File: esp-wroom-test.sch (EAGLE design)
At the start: 27 parts, among them IC1 TCAN1051HGV, U1 NCP1117LPST50T3G, U2 XN04312, U8 NCP1117LPST50T3G

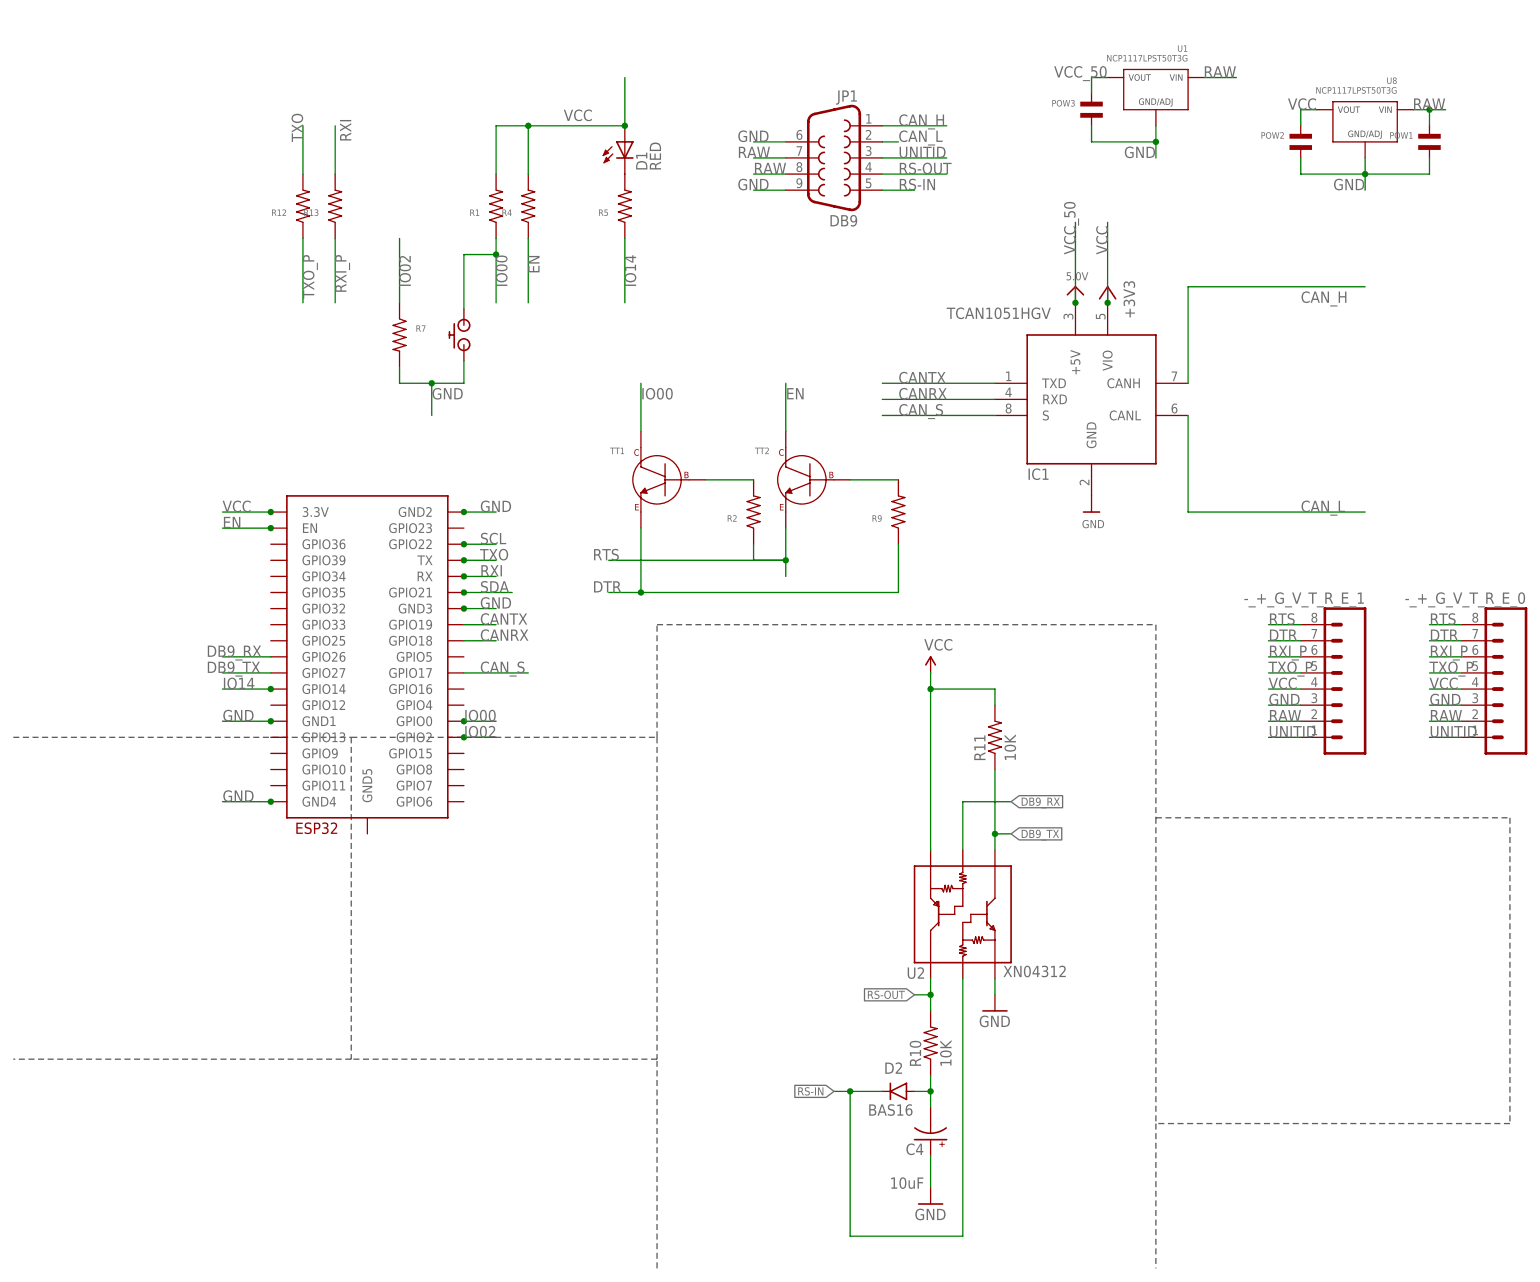
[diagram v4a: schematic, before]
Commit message: wroom test two sided
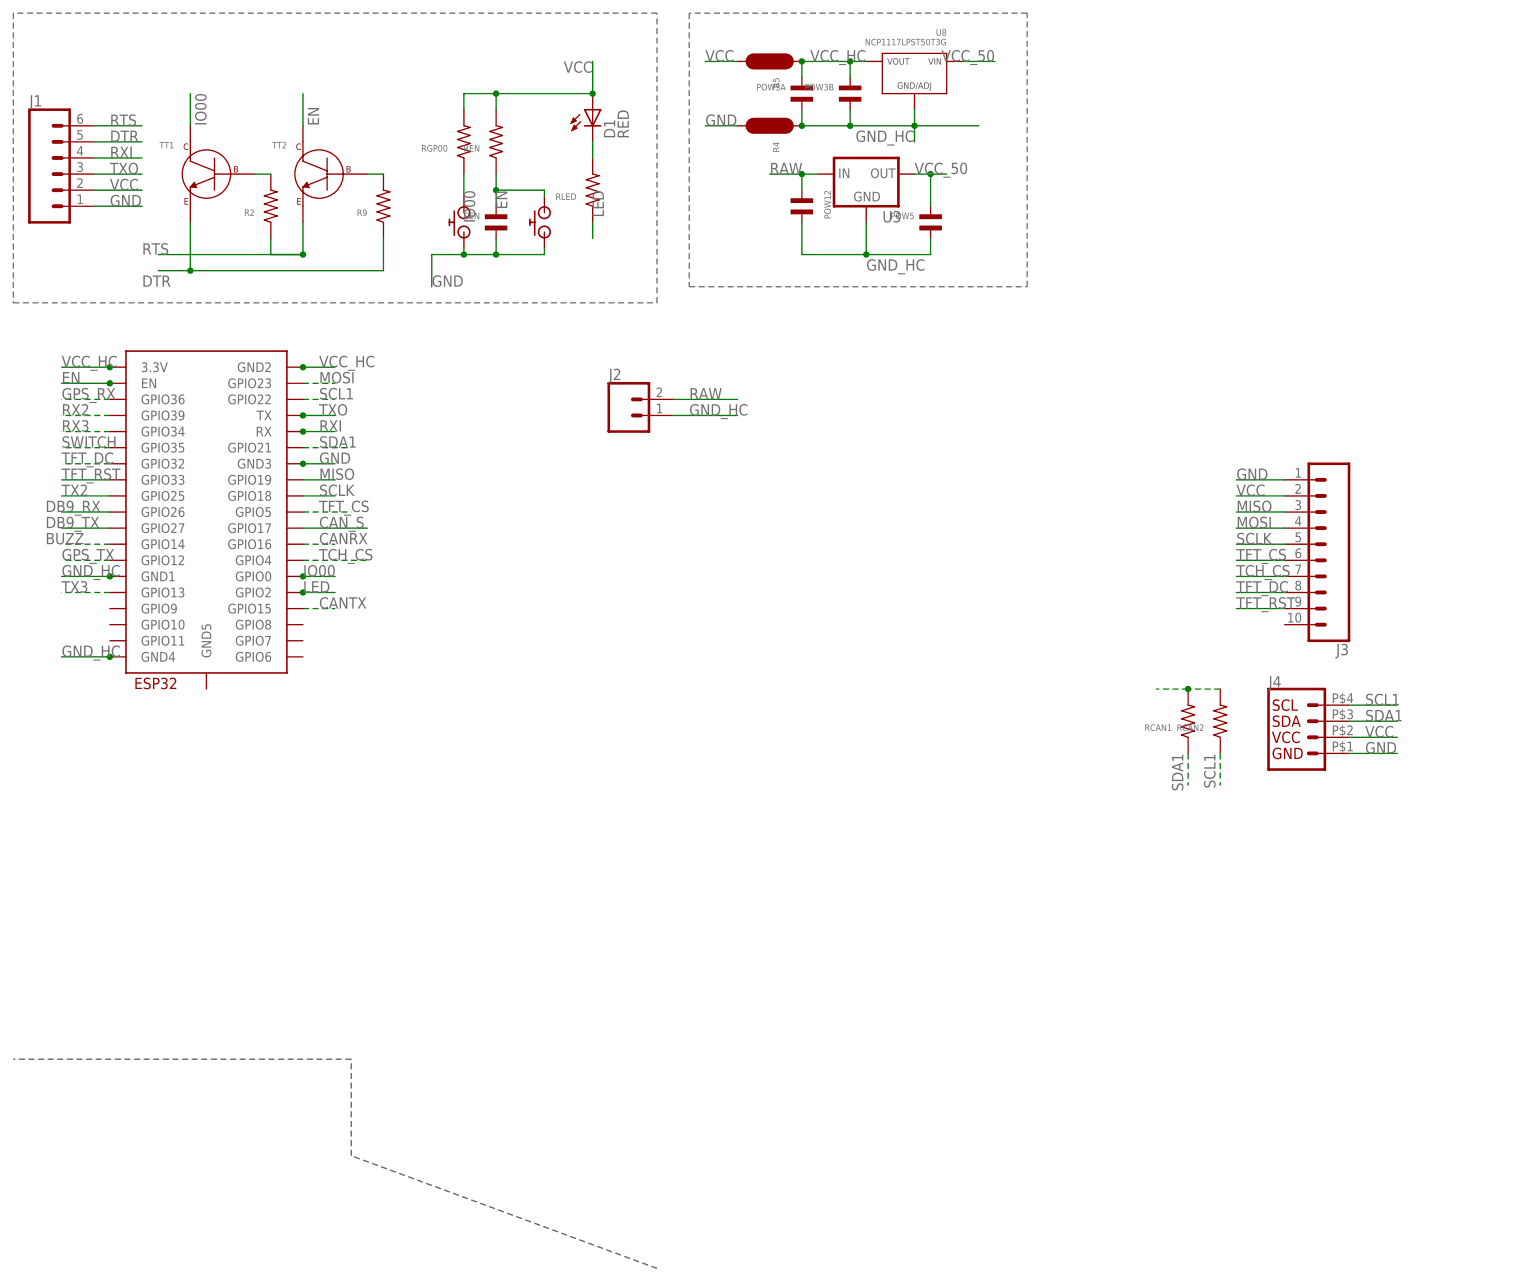
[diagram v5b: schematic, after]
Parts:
- removed -_+_G_V_T_R_E_0, -_+_G_V_T_R_E_1: MF-CON-2.54mm-01x08, SparkFun-Connectors:M081X08
- removed C4: 10uF, SparkFun-Capacitors:10UF-16V-10%(TANT)
- removed D2: BAS16, SparkFun-DiscreteSemi:DIODEBAS16
- removed IC1: TCAN1051HGV, microbuilder:CAN_TRANSCIEVER_TCAN1051V
- removed JP1: DB9, SparkFun-Connectors:DB9FEMALE
- removed POW1, POW2, POW3: (no value), MF_Passives:CAPACITOR_NP_1206
- removed R1, R12, R13, R7: (no value), 00jim:RESISTOR_0603
- removed R10, R11: 10K, SparkFun-Resistors:10KOHM1/10W1%(0603)0603
- removed U1: NCP1117LPST50T3G, MF_IC_Power:NCP1117LPST50T3G
- removed U2: XN04312, SparkFun-DiscreteSemi:XN04312SOT
- added CEN, POW12, POW3A, POW3B, POW5: (no value), MF_Passives:CAPACITOR_NP_0603
- added J1: (no value), 00jim:CONN_06
- added J2: (no value), SparkFun-Connectors:CONN_02
- added J3: (no value), SparkFun-Connectors:CONN_10
- added J4: Vertical Qwiic Connector, 00jim:QWIIC_CONNECTORJST04_1MM_HOLE
- added RCAN1, RCAN2, REN, RGP00, RLED: (no value), 00jim:RESISTOR_0603
- added U$2: AMAZON_BUTTONB2010, 00jim:AMAZON_BUTTONB2010
- added U3: (no value), SparkFun-IC-Power:V_REG_78XXSINK
- R4, R5: device 00jim:RESISTOR_0603 -> 00jim:JUMPER
- U$1: value AMAZON_BUTTON -> AMAZON_BUTTONB2010; device 00jim:AMAZON_BUTTON -> 00jim:AMAZON_BUTTONB2010
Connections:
- removed net CAN_H: IC1.CANH, JP1.1
- removed net CAN_L: IC1.CANL, JP1.2
- removed net IO02: R7.P$1, U$3.GPIO2
- removed net IO14: R5.P$1, U$3.GPIO14
- removed net N$4: C4.-, D2.A, R10.1
- removed net RS-IN: D2.C, JP1.5, U2.B1
- removed net RS-OUT: JP1.4, R10.2, U2.C2
- removed net RXI_P: -_+_G_V_T_R_E_0.6, -_+_G_V_T_R_E_1.6, R13.P$1
- removed net SCL: U$3.GPIO22
- removed net SDA: U$3.GPIO21
- removed net TXO_P: -_+_G_V_T_R_E_0.5, -_+_G_V_T_R_E_1.5, R12.P$1
- removed net UNITID: -_+_G_V_T_R_E_0.1, -_+_G_V_T_R_E_1.1, JP1.3
- new net BUZZ: U$3.GPIO14
- new net GND_HC: J2.1, POW12.P$2, POW3A.P$2, POW3B.P$2, POW5.P$2, R4.P$1, U$3.GND1, U$3.GND4, U3.GND, U8.GND/ADJ
- new net GPS_RX: U$3.GPIO36
- new net GPS_TX: U$3.GPIO12
- new net LED: RLED.P$1, U$3.GPIO2
- new net MISO: J3.3, U$3.GPIO19
- new net MOSI: J3.4, U$3.GPIO23
- new net RX2: U$3.GPIO39
- new net RX3: U$3.GPIO34
- new net SCL1: J4.4, RCAN2.P$1, U$3.GPIO22
- new net SCLK: J3.5, U$3.GPIO18
- new net SDA1: J4.3, RCAN1.P$1, U$3.GPIO21
- new net SWITCH: U$3.GPIO35
- new net TCH_CS: J3.7, U$3.GPIO4
- new net TFT_CS: J3.6, U$3.GPIO5
- new net TFT_DC: J3.8, U$3.GPIO32
- new net TFT_RST: J3.9, U$3.GPIO33
- new net TX2: U$3.GPIO25
- new net TX3: U$3.GPIO13
- new net VCC_HC: POW3A.P$1, POW3B.P$1, R5.P$1, U$3.3.3V, U$3.GND2, U8.VOUT
- net CANRX: now also U$3.GPIO16; no longer IC1.RXD, U$3.GPIO18
- net CANTX: now also U$3.GPIO15; no longer IC1.TXD, U$3.GPIO19
- net CAN_S: no longer IC1.S
- net DB9_RX: no longer U2.B2
- net DB9_TX: no longer R11.1, U2.C1
- net DTR: now also J1.5; no longer -_+_G_V_T_R_E_0.7, -_+_G_V_T_R_E_1.7
- net EN: now also CEN.P$1, REN.P$1, U$2.P$1; no longer R4.P$1
- net GND: now also CEN.P$2, J1.1, J3.1, J4.1, R4.P$2, U$2.P$2; no longer -_+_G_V_T_R_E_0.3, -_+_G_V_T_R_E_1.3, C4.+, IC1.GND, JP1.6, JP1.9, POW1.P$2, POW2.P$2, POW3.P$2, R7.P$2, U$3.GND1, U$3.GND2, U$3.GND4, U1.GND/ADJ, U2.E1, U8.GND/ADJ
- net IO00: now also RGP00.P$1; no longer R1.P$1
- net N$2: now also RLED.P$2; no longer R5.P$2
- net RAW: now also J2.2, POW12.P$1, U3.IN; no longer -_+_G_V_T_R_E_0.2, -_+_G_V_T_R_E_1.2, JP1.7, JP1.8, POW1.P$1, U1.VIN, U8.VIN
- net RTS: now also J1.6; no longer -_+_G_V_T_R_E_0.8, -_+_G_V_T_R_E_1.8
- net RXI: now also J1.4; no longer R13.P$2
- net TXO: now also J1.3; no longer R12.P$2
- net VCC: now also J1.2, J3.2, J4.2, R5.P$2, RCAN1.P$2, RCAN2.P$2, REN.P$2, RGP00.P$2; no longer -_+_G_V_T_R_E_0.4, -_+_G_V_T_R_E_1.4, IC1.VIO, POW2.P$1, R1.P$2, R11.2, R4.P$2, U$3.3.3V, U2.E2, U8.VOUT
- net VCC_50: now also POW5.P$1, U3.OUT, U8.VIN; no longer IC1.+5V, POW3.P$1, U1.VOUT
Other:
- moved on the sheet: D1, R2, R9, TT1, TT2, U8

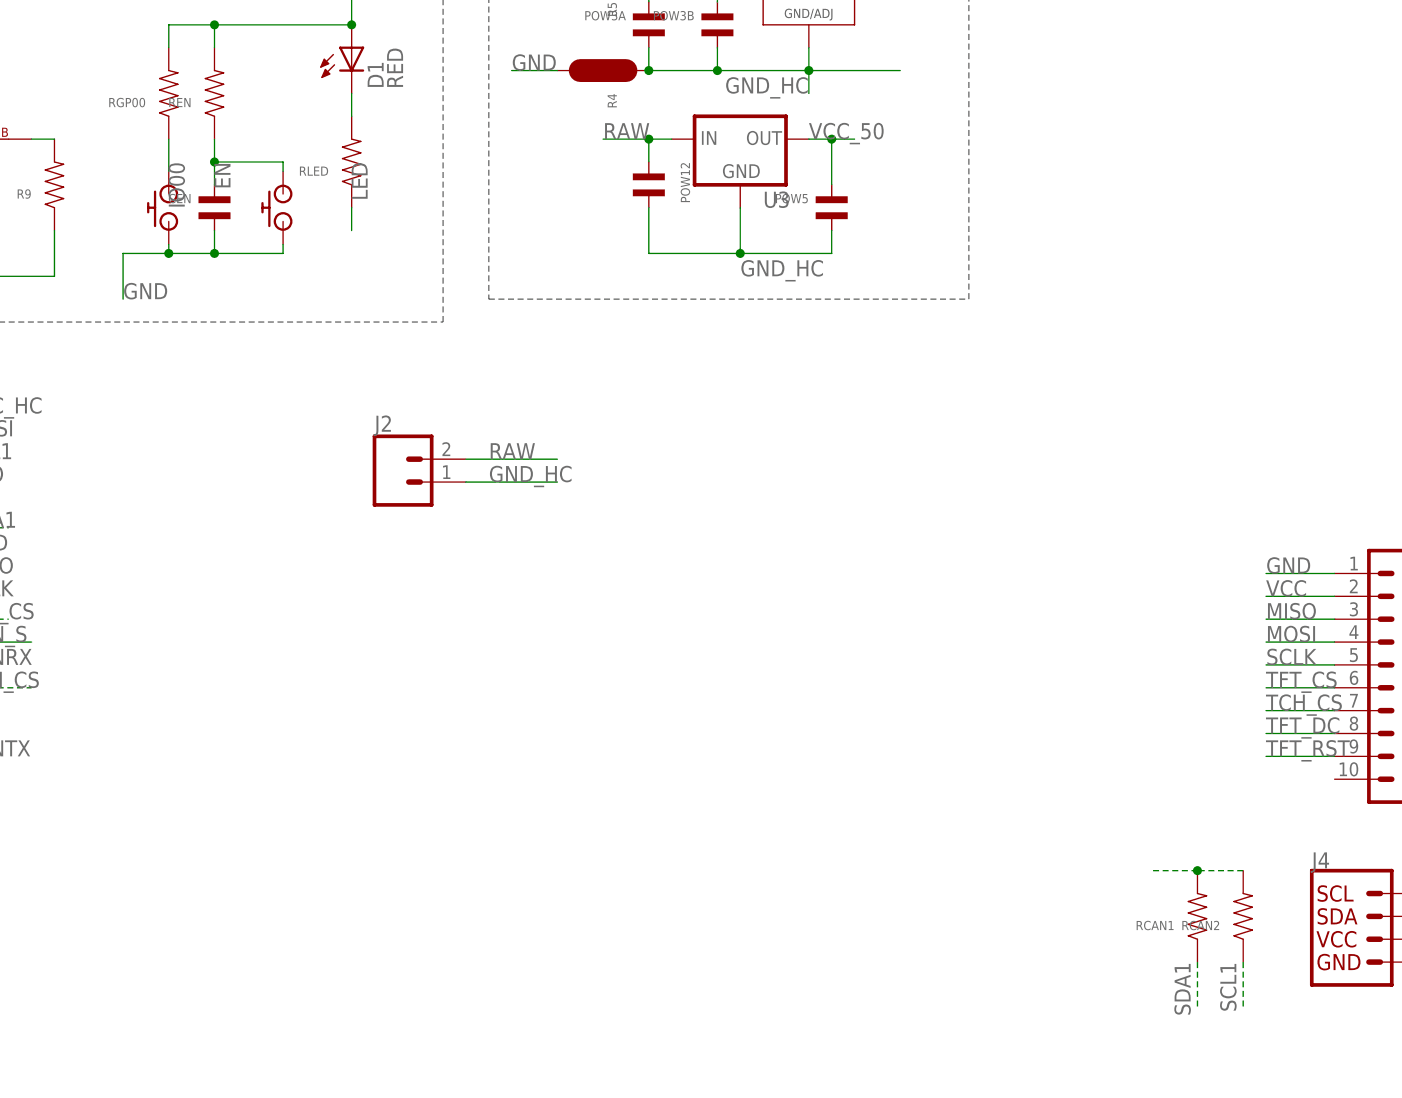
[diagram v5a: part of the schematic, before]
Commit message: Change wroom test to 12-06 resistors/leds
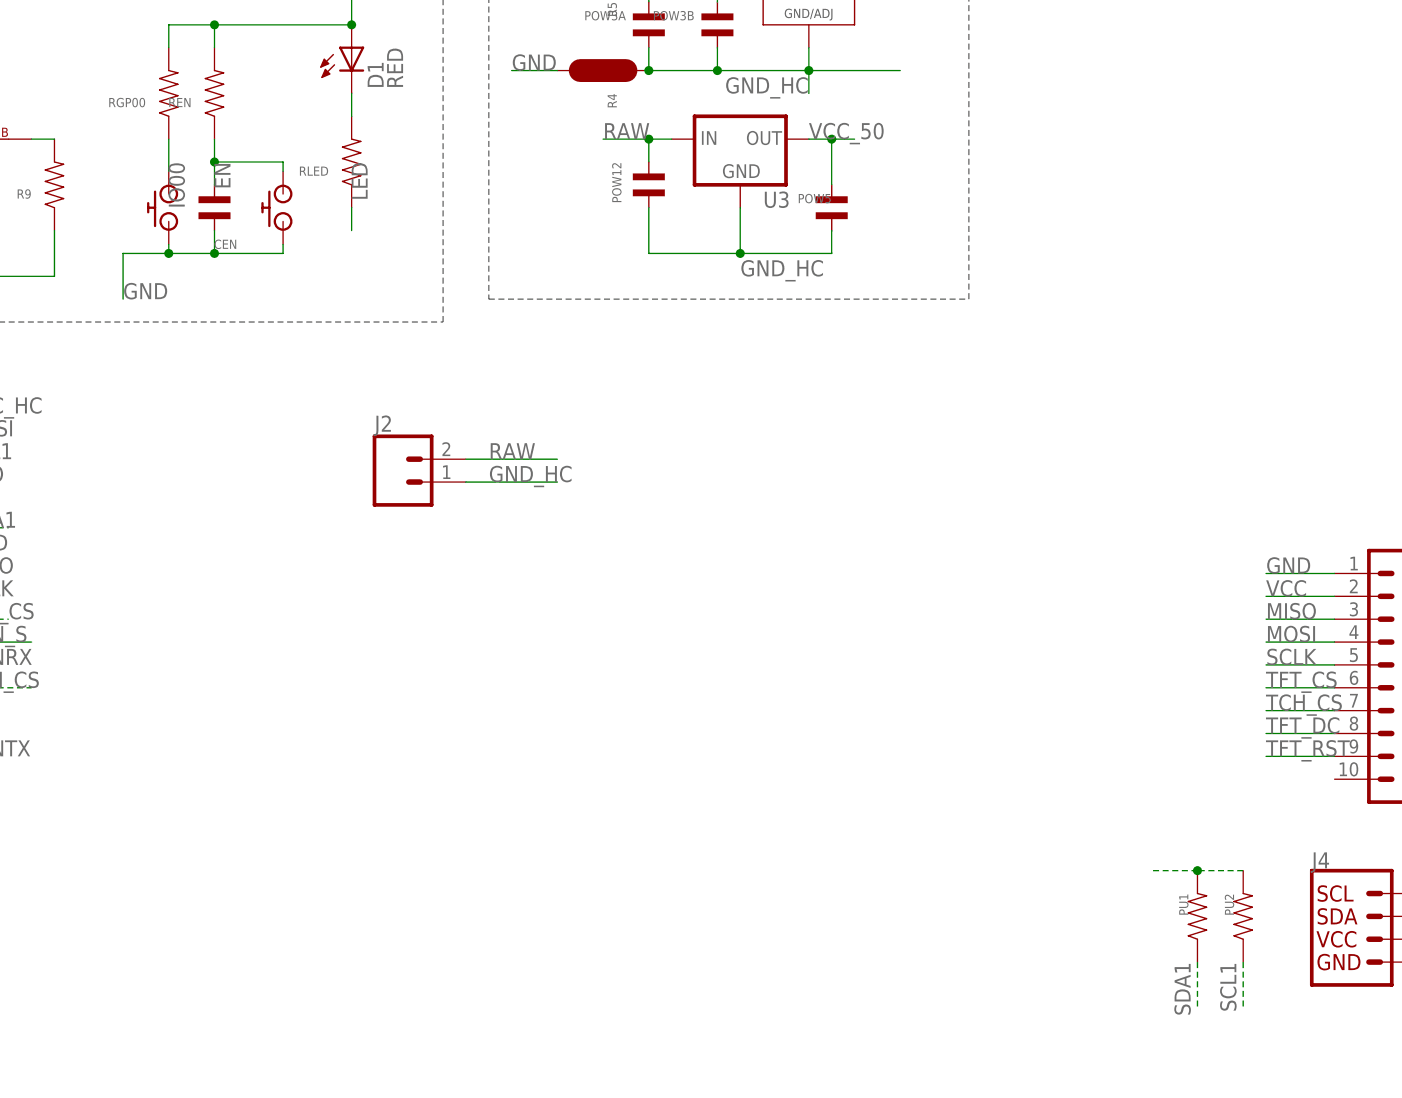
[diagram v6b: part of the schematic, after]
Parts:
- removed RCAN1, RCAN2: (no value), 00jim:RESISTOR_0603
- added PU1, PU2: (no value), 00jim:RESISTOR_1206
- CEN, POW12, POW3A, POW3B, POW5: device MF_Passives:CAPACITOR_NP_0603 -> MF_Passives:CAPACITOR_NP_1206
- D1: device 00jim:LED-RED0603 -> 00jim:LED-REDLILYPAD
- R2, R9, REN, RGP00, RLED: device 00jim:RESISTOR_0603 -> 00jim:RESISTOR_1206
- renumbered U$1 to SW2, U$2 to SW1
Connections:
- net SCL1: now also PU2.P$1; no longer RCAN2.P$1
- net SDA1: now also PU1.P$1; no longer RCAN1.P$1
- net VCC: now also PU1.P$2, PU2.P$2; no longer RCAN1.P$2, RCAN2.P$2
